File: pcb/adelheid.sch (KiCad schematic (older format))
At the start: 40 parts, among them J1 USB_B_Mini, J12 VCC, J13 D+, J14 D-, J15 GND, J2 MISO, J3 VCC, J4 SCK, J5 MOSI, J6 RES, J7 GND, J8 PF4, J9 PF5, Q1 2N7002, U1 USBLC6-2SC6, U2 ATmega32U4-AU, Y1 Crystal_GND24

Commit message: Updated schematic to replace Mini USB with USB-C and Add ARGB headers
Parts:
- removed J1: USB_B_Mini, Keebio-Parts:USB-Mini-B_2leg, symbol Connector:USB_B_Micro
- removed J12, J3: VCC, Pin_Headers:Pin_Header_Straight_1x01_Pitch2.54mm, symbol Connector_Generic:Conn_01x01
- removed J13: D+, Pin_Headers:Pin_Header_Straight_1x01_Pitch2.54mm, symbol Connector_Generic:Conn_01x01
- removed J14: D-, Pin_Headers:Pin_Header_Straight_1x01_Pitch2.54mm, symbol Connector_Generic:Conn_01x01
- removed J15, J7: GND, Pin_Headers:Pin_Header_Straight_1x01_Pitch2.54mm, symbol Connector_Generic:Conn_01x01
- removed J2: MISO, Pin_Headers:Pin_Header_Straight_1x01_Pitch2.54mm, symbol Connector_Generic:Conn_01x01
- removed J4: SCK, Pin_Headers:Pin_Header_Straight_1x01_Pitch2.54mm, symbol Connector_Generic:Conn_01x01
- removed J5: MOSI, Pin_Headers:Pin_Header_Straight_1x01_Pitch2.54mm, symbol Connector_Generic:Conn_01x01
- removed J6: RES, Pin_Headers:Pin_Header_Straight_1x01_Pitch2.54mm, symbol Connector_Generic:Conn_01x01
- removed J8: PF4, Pin_Headers:Pin_Header_Straight_1x01_Pitch2.54mm, symbol Connector_Generic:Conn_01x01
- removed J9: PF5, Pin_Headers:Pin_Header_Straight_1x01_Pitch2.54mm, symbol Connector_Generic:Conn_01x01
- added J1: USB_C_Receptacle_HRO_TYPE-C-31-M-12, symbol USB_Type-C:USB_C_Receptacle_HRO_TYPE-C-31-M-12
- added J2, J3: Conn_01x06, symbol Connector_Generic:Conn_01x06
- added J4: RGB, symbol Connector_Generic:Conn_01x03
- added J5: RGB_IN, symbol Connector_Generic:Conn_01x03
- added J6: RGB_OUT, symbol Connector_Generic:Conn_01x03
- added R6, R7: 5k1, Resistor_SMD:R_0805_2012Metric_Pad1.20x1.40mm_HandSolder, symbol Device:R
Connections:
- net labels added: RBG_A, RESET, RGB, RGB_A, SCLK, USB+, USB-
- net labels removed: SCK, ~RES~
- wire segments 143 -> 127
- no-connect marks 4 -> 3
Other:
- note added: "ARGB Strip Headers"
- note added: "USB & Programming Headers"
- note added: "USB-C Connection & ESP Protection"
- moved on the sheet: R1, R2, U1

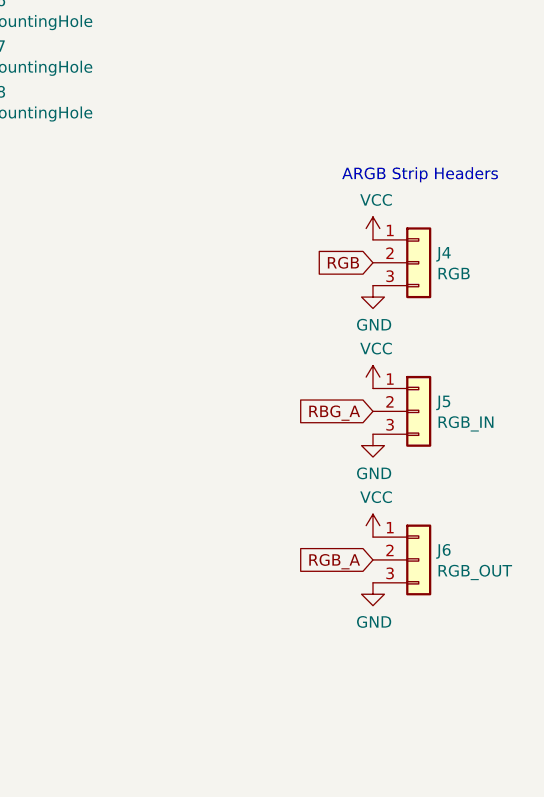
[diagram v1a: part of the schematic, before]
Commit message: Replace single colour underglow and RGB headers for WS2812B Addressable SMD LED
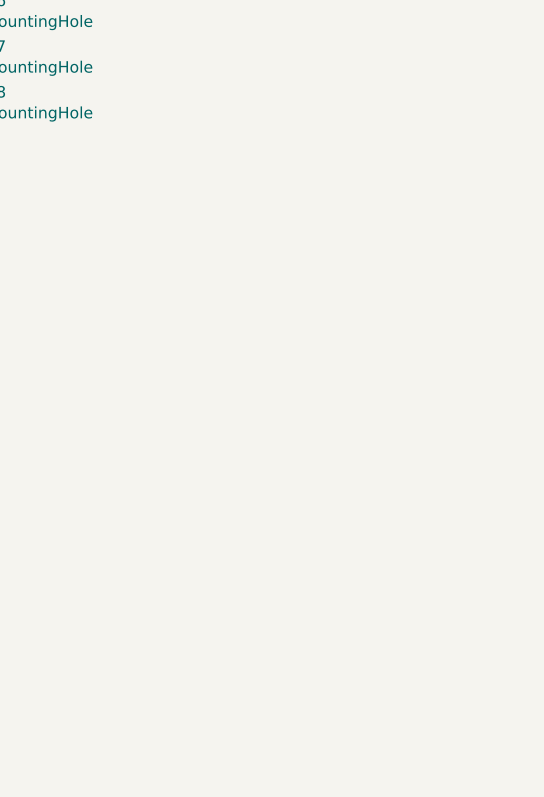
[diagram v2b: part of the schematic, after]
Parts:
- removed J4: RGB, symbol Connector_Generic:Conn_01x03
- removed J5: RGB_IN, symbol Connector_Generic:Conn_01x03
- removed J6: RGB_OUT, symbol Connector_Generic:Conn_01x03
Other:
- note removed: "ARGB Strip Headers"

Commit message: Update all components with JLCPCB part numbers
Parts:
- C1, C2: LCSC (none) -> C1804
- C3: LCSC (none) -> C15850
- C4, C5: LCSC (none) -> C28323
- C6, C7, C8, C9: LCSC (none) -> C49678
- Q1: LCSC (none) -> C8545
- R1, R2: LCSC (none) -> C17561
- R3, R4: LCSC (none) -> C17414
- R5: LCSC (none) -> C4310
- R6, R7: LCSC (none) -> C27834
- SWR1: LCSC (none) -> C318884
- U1: LCSC (none) -> C7519
- U2: LCSC (none) -> C44854
- Y1: LCSC (none) -> C13738
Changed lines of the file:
@@
 F 2 "Housings_QFP:TQFP-44_10x10mm_Pitch0.8mm" H 4500 4250 50  0001 C CIN
 F 3 "http://ww1.microchip.com/downloads/en/DeviceDoc/Atmel-7766-8-bit-AVR-ATmega16U4-32U4_Datasheet.pdf" H 4500 4250 50  0001 C CNN
+F 4 "C44854" H 4500 4250 50  0001 C CNN "LCSC"
 	1    4500 4250
 	1    0    0    -1
@@
 F 2 "Resistor_SMD:R_0805_2012Metric_Pad1.15x1.40mm_HandSolder" V 2980 6100 50  0001 C CNN
 F 3 "~" H 3050 6100 50  0001 C CNN
+F 4 "C17561" H 3050 6100 50  0001 C CNN "LCSC"
 	1    3050 6100
 	0    1    1    0
@@
 F 2 "Capacitors_SMD:C_0805_HandSoldering" H 3688 4050 50  0001 C CNN
 F 3 "~" H 3650 4200 50  0001 C CNN
+F 4 "C28323" H 3650 4200 50  0001 C CNN "LCSC"
 	1    3650 4200
 	1    0    0    -1
@@
 F 2 "Crystals:Crystal_SMD_SeikoEpson_FA238-4pin_3.2x2.5mm_HandSoldering" H 1900 3650 50  0001 C CNN
 F 3 "~" H 1900 3650 50  0001 C CNN
+F 4 "C13738" H 1900 3650 50  0001 C CNN "LCSC"
 	1    1900 3650
 	1    0    0    -1
@@
 F 2 "Capacitors_SMD:C_0805_HandSoldering" H 1588 3650 50  0001 C CNN
 F 3 "~" H 1550 3800 50  0001 C CNN
+F 4 "C1804" H 1550 3800 50  0001 C CNN "LCSC"
 	1    1550 3800
 	1    0    0    1
@@
 F 2 "Capacitors_SMD:C_0805_HandSoldering" H 2288 3650 50  0001 C CNN
 F 3 "~" H 2250 3800 50  0001 C CNN
+F 4 "C1804" H 2250 3800 50  0001 C CNN "LCSC"
 	1    2250 3800
 	1    0    0    -1
@@
 F 2 "Capacitors_SMD:C_0805_HandSoldering" H 3288 4050 50  0001 C CNN
 F 3 "~" H 3250 4200 50  0001 C CNN
+F 4 "C15850" H 3250 4200 50  0001 C CNN "LCSC"
 	1    3250 4200
 	1    0    0    -1
@@
 F 2 "Buttons_Switches_SMD:SW_SPST_TL3342" H 3400 2950 50  0001 C CNN
 F 3 "" H 3400 2950 50  0001 C CNN
+F 4 "C318884" H 3400 2750 50  0001 C CNN "LCSC"
 	1    3400 2750
 	1    0    0    -1
@@
 F 2 "Resistor_SMD:R_0805_2012Metric_Pad1.15x1.40mm_HandSolder" V 3730 2550 50  0001 C CNN
 F 3 "~" H 3800 2550 50  0001 C CNN
+F 4 "C17414" H 3800 2550 50  0001 C CNN "LCSC"
 	1    3800 2550
 	1    0    0    -1
@@
 F 2 "Capacitors_SMD:C_0805_HandSoldering" H 5288 1000 50  0001 C CNN
 F 3 "~" H 5250 1150 50  0001 C CNN
+F 4 "C28323" H 5250 1150 50  0001 C CNN "LCSC"
 	1    5250 1150
 	1    0    0    -1
@@
 F 2 "Capacitors_SMD:C_0805_HandSoldering" H 5288 1550 50  0001 C CNN
 F 3 "~" H 5250 1700 50  0001 C CNN
+F 4 "C49678" H 5250 1700 50  0001 C CNN "LCSC"
 	1    5250 1700
 	1    0    0    -1
@@
 F 2 "Capacitors_SMD:C_0805_HandSoldering" H 5738 1550 50  0001 C CNN
 F 3 "~" H 5700 1700 50  0001 C CNN
+F 4 "C49678" H 5700 1700 50  0001 C CNN "LCSC"
 	1    5700 1700
 	1    0    0    -1
@@
 F 2 "Capacitors_SMD:C_0805_HandSoldering" H 5288 2100 50  0001 C CNN
 F 3 "~" H 5250 2250 50  0001 C CNN
+F 4 "C49678" H 5250 2250 50  0001 C CNN "LCSC"
 	1    5250 2250
 	1    0    0    -1
@@
 F 2 "Capacitors_SMD:C_0805_HandSoldering" H 5738 2100 50  0001 C CNN
 F 3 "~" H 5700 2250 50  0001 C CNN
+F 4 "C49678" H 5700 2250 50  0001 C CNN "LCSC"
 	1    5700 2250
 	1    0    0    -1
@@
 F 2 "Resistor_SMD:R_0805_2012Metric_Pad1.15x1.40mm_HandSolder" V 5630 5900 50  0001 C CNN
 F 3 "~" H 5700 5900 50  0001 C CNN
+F 4 "C17414" H 5700 5900 50  0001 C CNN "LCSC"
 	1    5700 5900
 	1    0    0    -1
@@
 F 2 "Package_TO_SOT_SMD:SOT-23" H 6550 5875 50  0001 L CIN
 F 3 "https://www.fairchildsemi.com/datasheets/2N/2N7002.pdf" H 6350 5950 50  0001 L CNN
+F 4 "C8545" H 6350 5950 50  0001 C CNN "LCSC"
 	1    6350 5950
 	1    0    0    -1
@@
 F 2 "Resistor_SMD:R_0805_2012Metric_Pad1.15x1.40mm_HandSolder" V 5530 3650 50  0001 C CNN
 F 3 "~" H 5600 3650 50  0001 C CNN
+F 4 "C4310" H 5600 3650 50  0001 C CNN "LCSC"
 	1    5600 3650
 	0    -1   -1   0
@@
 F 2 "Resistor_SMD:R_0805_2012Metric_Pad1.15x1.40mm_HandSolder" V 2980 7100 50  0001 C CNN
 F 3 "~" H 3050 7100 50  0001 C CNN
+F 4 "C17561" H 3050 7100 50  0001 C CNN "LCSC"
 	1    3050 7100
 	0    1    1    0
@@
 F 2 "TO_SOT_Packages_SMD:SOT-23-6_Handsoldering" H 2050 7000 50  0001 C CNN
 F 3 "http://www2.st.com/resource/en/datasheet/CD00050750.pdf" H 3000 6950 50  0001 C CNN
+F 4 "C7519" H 2800 6600 50  0001 C CNN "LCSC"
 	1    2800 6600
 	0    1    1    0
@@
 F 2 "Resistor_SMD:R_0805_2012Metric_Pad1.20x1.40mm_HandSolder" V 1980 6200 50  0001 C CNN
 F 3 "~" H 2050 6200 50  0001 C CNN
+F 4 "C27834" H 2050 6200 50  0001 C CNN "LCSC"
 	1    2050 6200
 	0    1    1    0
@@
 F 2 "Resistor_SMD:R_0805_2012Metric_Pad1.20x1.40mm_HandSolder" V 1730 6300 50  0001 C CNN
 F 3 "~" H 1800 6300 50  0001 C CNN
+F 4 "C27834" H 1800 6300 50  0001 C CNN "LCSC"
 	1    1800 6300
 	0    -1   -1   0

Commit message: Fix missing footprints
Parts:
- J1: footprint (none) -> adelheid:USB_C_Receptacle_HRO_TYPE-C-31-M-12-HandSoldering
- J2, J3: footprint (none) -> Connector_PinHeader_2.54mm:PinHeader_1x06_P2.54mm_Vertical
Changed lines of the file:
@@
 F 0 "J1" H 1157 7467 50  0000 C CNN
 F 1 "USB_C_Receptacle_HRO_TYPE-C-31-M-12" H 600 7350 50  0000 L CNN
-F 2 "" H 1200 6600 50  0001 C CNN
+F 2 "adelheid:USB_C_Receptacle_HRO_TYPE-C-31-M-12-HandSoldering" H 1200 6600 50  0001 C CNN
 F 3 "" H 1200 6600 50  0001 C CNN
 	1    1050 6600
@@
 F 0 "J2" H 9430 1342 50  0000 L CNN
 F 1 "Conn_01x06" H 9430 1251 50  0000 L CNN
-F 2 "" H 9350 1350 50  0001 C CNN
+F 2 "Connector_PinHeader_2.54mm:PinHeader_1x06_P2.54mm_Vertical" H 9350 1350 50  0001 C CNN
 F 3 "~" H 9350 1350 50  0001 C CNN
 	1    9350 1350
@@
 F 0 "J3" H 10430 1342 50  0000 L CNN
 F 1 "Conn_01x06" H 10430 1251 50  0000 L CNN
-F 2 "" H 10350 1350 50  0001 C CNN
+F 2 "Connector_PinHeader_2.54mm:PinHeader_1x06_P2.54mm_Vertical" H 10350 1350 50  0001 C CNN
 F 3 "~" H 10350 1350 50  0001 C CNN
 	1    10350 1350

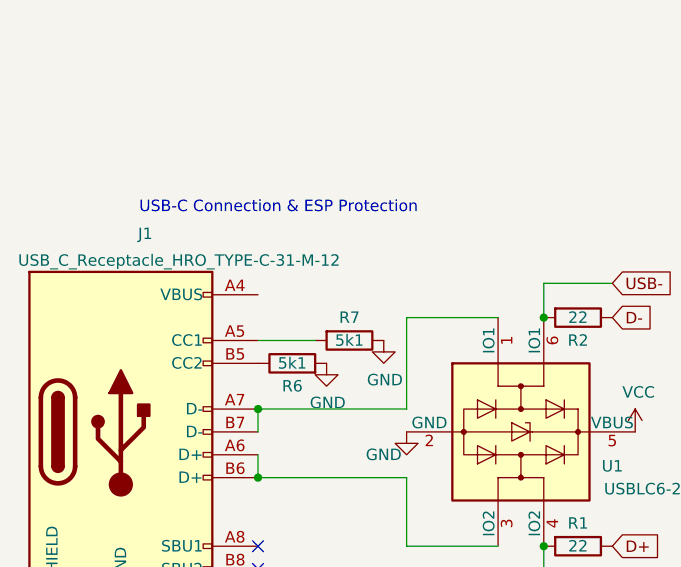
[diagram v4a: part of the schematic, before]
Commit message: Fixed missing VCC for USB connector and incorrect DIN/DOUT for underground LED's
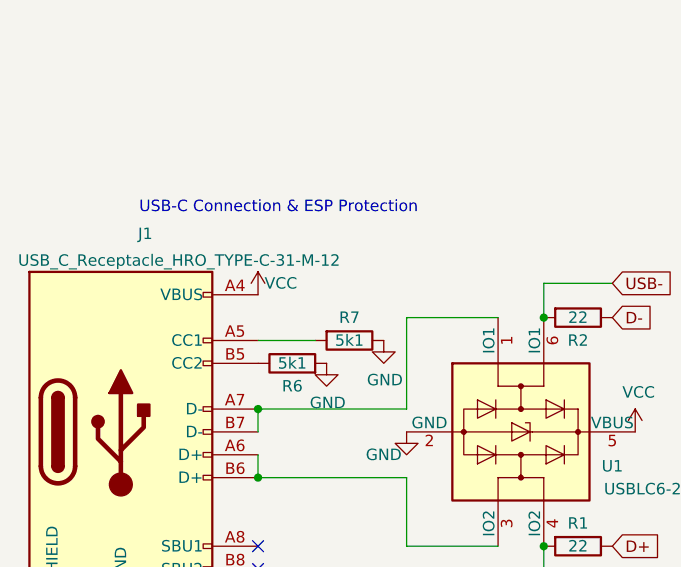
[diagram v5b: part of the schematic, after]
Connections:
- net VCC: now also J1.A4 (VBUS), J1.A9 (VBUS)
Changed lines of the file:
@@
 Wire Bus Line
 	7050 2650 7050 5800
+$Comp
+L power:VCC #PWR0103
+U 1 1 67AEB0EF
+P 1650 6000
+F 0 "#PWR0103" H 1650 5850 50  0001 C CNN
+F 1 "VCC" H 1750 6050 50  0000 C CNN
+F 2 "" H 1650 6000 50  0001 C CNN
+F 3 "" H 1650 6000 50  0001 C CNN
+	1    1650 6000
+	1    0    0    -1
+$EndComp
 $EndSCHEMATC

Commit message: Regenerate all files to for release to JLCPCB
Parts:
- J1: LCSC (none) -> C319148
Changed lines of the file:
@@
 F 2 "adelheid:USB_C_Receptacle_HRO_TYPE-C-31-M-12-HandSoldering" H 1200 6600 50  0001 C CNN
 F 3 "" H 1200 6600 50  0001 C CNN
+F 4 "C319148" H 1050 6600 50  0001 C CNN "LCSC"
 	1    1050 6600
 	1    0    0    -1
